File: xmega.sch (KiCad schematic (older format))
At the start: 30 parts, among them J1 USB, J2 PORTA, J4 PORTB, J5 PORTC, J6 PORTE, U1 ATXMEGA128A1U-AU, U5 M24C02-WDW6TP, U6 ADR380

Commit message: Finished?
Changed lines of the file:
@@
 $EndComp
 $Comp
-L GND #PWR3
+L GND #PWR2
 U 1 1 56EBAB34
 P 1300 7400
-F 0 "#PWR3" H 1300 7400 30  0001 C CNN
+F 0 "#PWR2" H 1300 7400 30  0001 C CNN
 F 1 "GND" H 1300 7330 30  0001 C CNN
 F 2 "" H 1300 7400 60  0000 C CNN
@@
 $EndComp
 $Comp
-L GND #PWR21
+L GND #PWR18
 U 1 1 56ECF12E
 P 9950 5000
-F 0 "#PWR21" H 9950 5000 30  0001 C CNN
+F 0 "#PWR18" H 9950 5000 30  0001 C CNN
 F 1 "GND" H 9950 4930 30  0001 C CNN
 F 2 "" H 9950 5000 60  0000 C CNN
@@
 $EndComp
 $Comp
-L +3.3 #PWR20
+L +3.3 #PWR17
 U 1 1 56F51703
 P 9950 4450
-F 0 "#PWR20" H 9950 4500 30  0001 C CNN
+F 0 "#PWR17" H 9950 4500 30  0001 C CNN
 F 1 "+3.3" H 9950 4583 50  0000 C CNN
 F 2 "" H 9950 4450 60  0000 C CNN
@@
 	1150 7200 1300 7200
 Wire Wire Line
-	1300 7200 1300 7300
-Wire Wire Line
-	1300 7300 1300 7400
+	1300 7200 1300 7400
 Wire Wire Line
 	1300 7300 1200 7300
@@
 	9950 5000 9950 4950
 Wire Wire Line
-	7500 3700 7800 3700
-Wire Wire Line
-	7800 3700 8000 3700
+	7500 3700 8000 3700
 Connection ~ 7800 3700
 Wire Wire Line
@@
 	7950 4100 7800 4100
 Wire Wire Line
-	7800 4000 7800 4100
-Wire Wire Line
-	7800 4100 7800 4150
-$Comp
-L GND #PWR30
+	7800 4000 7800 4150
+$Comp
+L GND #PWR15
 U 1 1 56EF0C92
 P 7800 4150
-F 0 "#PWR30" H 7800 4150 30  0001 C CNN
+F 0 "#PWR15" H 7800 4150 30  0001 C CNN
 F 1 "GND" H 7800 4080 30  0001 C CNN
 F 2 "" H 7800 4150 60  0000 C CNN
@@
 	8800 3500 8900 3500
 Wire Wire Line
-	8900 3500 8900 3600
-Wire Wire Line
-	8900 3600 8900 3700
-Wire Wire Line
-	8900 3700 8900 3800
-Wire Wire Line
-	8900 3800 8900 3850
-$Comp
-L GND #PWR40
+	8900 3500 8900 3850
+$Comp
+L GND #PWR16
 U 1 1 56EF1A27
 P 8900 3850
-F 0 "#PWR40" H 8900 3850 30  0001 C CNN
+F 0 "#PWR16" H 8900 3850 30  0001 C CNN
 F 1 "GND" H 8900 3780 30  0001 C CNN
 F 2 "" H 8900 3850 60  0000 C CNN
@@
 P 2400 5300
 AR Path="/56EF5090/56EFEF42" Ref="#PWR?"  Part="1"
-AR Path="/56EFEF42" Ref="#PWR?"  Part="1"
-F 0 "#PWR?" H 2400 5300 30  0001 C CNN
+AR Path="/56EFEF42" Ref="#PWR11"  Part="1"
+F 0 "#PWR11" H 2400 5300 30  0001 C CNN
 F 1 "GND" H 2400 5230 30  0001 C CNN
 F 2 "" H 2400 5300 60  0000 C CNN
@@
 P 2400 4400
 AR Path="/56EF5090/56EFEF48" Ref="#PWR?"  Part="1"
-AR Path="/56EFEF48" Ref="#PWR?"  Part="1"
-F 0 "#PWR?" H 2400 4400 30  0001 C CNN
+AR Path="/56EFEF48" Ref="#PWR10"  Part="1"
+F 0 "#PWR10" H 2400 4400 30  0001 C CNN
 F 1 "GND" H 2400 4330 30  0001 C CNN
 F 2 "" H 2400 4400 60  0000 C CNN
@@
 P 2400 6500
 AR Path="/56EF5090/56EFEF66" Ref="#PWR?"  Part="1"
-AR Path="/56EFEF66" Ref="#PWR?"  Part="1"
-F 0 "#PWR?" H 2400 6500 30  0001 C CNN
+AR Path="/56EFEF66" Ref="#PWR13"  Part="1"
+F 0 "#PWR13" H 2400 6500 30  0001 C CNN
 F 1 "GND" H 2400 6430 30  0001 C CNN
 F 2 "" H 2400 6500 60  0000 C CNN
@@
 P 2400 5600
 AR Path="/56EF5090/56EFEF6C" Ref="#PWR?"  Part="1"
-AR Path="/56EFEF6C" Ref="#PWR?"  Part="1"
-F 0 "#PWR?" H 2400 5600 30  0001 C CNN
+AR Path="/56EFEF6C" Ref="#PWR12"  Part="1"
+F 0 "#PWR12" H 2400 5600 30  0001 C CNN
 F 1 "GND" H 2400 5530 30  0001 C CNN
 F 2 "" H 2400 5600 60  0000 C CNN
@@
 PA7
 $Comp
-L GND #PWR?
+L GND #PWR7
 U 1 1 56EFF0A4
 P 2400 1700
-AR Path="/56EFF0A4" Ref="#PWR?"  Part="1"
+AR Path="/56EFF0A4" Ref="#PWR7"  Part="1"
 AR Path="/56EF5090/56EFF0A4" Ref="#PWR?"  Part="1"
-F 0 "#PWR?" H 2400 1700 30  0001 C CNN
+F 0 "#PWR7" H 2400 1700 30  0001 C CNN
 F 1 "GND" H 2400 1630 30  0001 C CNN
 F 2 "" H 2400 1700 60  0000 C CNN
@@
 $EndComp
 $Comp
-L GND #PWR?
+L GND #PWR6
 U 1 1 56EFF0AA
 P 2400 800
-AR Path="/56EFF0AA" Ref="#PWR?"  Part="1"
+AR Path="/56EFF0AA" Ref="#PWR6"  Part="1"
 AR Path="/56EF5090/56EFF0AA" Ref="#PWR?"  Part="1"
-F 0 "#PWR?" H 2400 800 30  0001 C CNN
+F 0 "#PWR6" H 2400 800 30  0001 C CNN
 F 1 "GND" H 2400 730 30  0001 C CNN
 F 2 "" H 2400 800 60  0000 C CNN
@@
 $EndComp
 $Comp
-L GND #PWR?
+L GND #PWR9
 U 1 1 56EFF0C0
 P 2400 3000
-AR Path="/56EFF0C0" Ref="#PWR?"  Part="1"
+AR Path="/56EFF0C0" Ref="#PWR9"  Part="1"
 AR Path="/56EF5090/56EFF0C0" Ref="#PWR?"  Part="1"
-F 0 "#PWR?" H 2400 3000 30  0001 C CNN
+F 0 "#PWR9" H 2400 3000 30  0001 C CNN
 F 1 "GND" H 2400 2930 30  0001 C CNN
 F 2 "" H 2400 3000 60  0000 C CNN
@@
 $EndComp
 $Comp
-L GND #PWR?
+L GND #PWR8
 U 1 1 56EFF0C6
 P 2400 2100
-AR Path="/56EFF0C6" Ref="#PWR?"  Part="1"
+AR Path="/56EFF0C6" Ref="#PWR8"  Part="1"
 AR Path="/56EF5090/56EFF0C6" Ref="#PWR?"  Part="1"
-F 0 "#PWR?" H 2400 2100 30  0001 C CNN
+F 0 "#PWR8" H 2400 2100 30  0001 C CNN
 F 1 "GND" H 2400 2030 30  0001 C CNN
 F 2 "" H 2400 2100 60  0000 C CNN
@@
 $EndComp
 $Comp
-L GND #PWR?
+L GND #PWR1
 U 1 1 56EFF0E4
 P 900 3750
-AR Path="/56EFF0E4" Ref="#PWR?"  Part="1"
+AR Path="/56EFF0E4" Ref="#PWR1"  Part="1"
 AR Path="/56EF5090/56EFF0E4" Ref="#PWR?"  Part="1"
-F 0 "#PWR?" H 900 3750 30  0001 C CNN
+F 0 "#PWR1" H 900 3750 30  0001 C CNN
 F 1 "GND" H 900 3680 30  0001 C CNN
 F 2 "" H 900 3750 60  0000 C CNN
@@
 $EndComp
 $Comp
-L GND #PWR?
+L GND #PWR3
 U 1 1 56EFF0EA
 P 1400 3750
-AR Path="/56EFF0EA" Ref="#PWR?"  Part="1"
+AR Path="/56EFF0EA" Ref="#PWR3"  Part="1"
 AR Path="/56EF5090/56EFF0EA" Ref="#PWR?"  Part="1"
-F 0 "#PWR?" H 1400 3750 30  0001 C CNN
+F 0 "#PWR3" H 1400 3750 30  0001 C CNN
 F 1 "GND" H 1400 3680 30  0001 C CNN
 F 2 "" H 1400 3750 60  0000 C CNN
@@
 PB0
 $Comp
-L GND #PWR?
+L GND #PWR4
 U 1 1 56EFF10A
 P 1800 4150
-AR Path="/56EFF10A" Ref="#PWR?"  Part="1"
+AR Path="/56EFF10A" Ref="#PWR4"  Part="1"
 AR Path="/56EF5090/56EFF10A" Ref="#PWR?"  Part="1"
-F 0 "#PWR?" H 1800 4150 30  0001 C CNN
+F 0 "#PWR4" H 1800 4150 30  0001 C CNN
 F 1 "GND" H 1800 4080 30  0001 C CNN
 F 2 "" H 1800 4150 60  0000 C CNN
@@
 $EndComp
 $Comp
-L GND #PWR?
+L GND #PWR5
 U 1 1 56EFF118
 P 2250 4150
-AR Path="/56EFF118" Ref="#PWR?"  Part="1"
+AR Path="/56EFF118" Ref="#PWR5"  Part="1"
 AR Path="/56EF5090/56EFF118" Ref="#PWR?"  Part="1"
-F 0 "#PWR?" H 2250 4150 30  0001 C CNN
+F 0 "#PWR5" H 2250 4150 30  0001 C CNN
 F 1 "GND" H 2250 4080 30  0001 C CNN
 F 2 "" H 2250 4150 60  0000 C CNN
@@
 $EndComp
 Wire Wire Line
-	1950 900  2250 900
-Wire Wire Line
-	2250 900  2450 900
+	1950 900  2450 900
 Wire Wire Line
 	2450 1000 1950 1000
@@
 	2400 800  2450 800
 Wire Wire Line
-	1950 2200 2300 2200
-Wire Wire Line
-	2300 2200 2450 2200
+	1950 2200 2450 2200
 Wire Wire Line
 	2450 2300 1950 2300
@@
 	1050 3400 900  3400
 Wire Wire Line
-	900  3300 900  3400
-Wire Wire Line
-	900  3400 900  3500
+	900  3300 900  3500
 Wire Wire Line
 	900  3750 900  3700
@@
 Connection ~ 900  3400
 Wire Wire Line
-	1750 3400 1800 3400
-Wire Wire Line
-	1800 3400 1850 3400
+	1750 3400 1850 3400
 Wire Wire Line
 	1850 3800 1800 3800
 Wire Wire Line
-	1800 3400 1800 3800
-Wire Wire Line
-	1800 3800 1800 3900
+	1800 3400 1800 3900
 Connection ~ 1800 3400
 Wire Wire Line
@@
 	3100 2860 7300 2860
 Wire Wire Line
-	1150 6800 1700 6800
-Wire Wire Line
-	1700 6800 9100 6800
+	1150 6800 9100 6800
 $Comp
 L DRTR5V0U2SR DZ1
@@
 $EndComp
 Wire Wire Line
-	1150 6900 2250 6900
-Wire Wire Line
-	2250 6900 3100 6900
+	1150 6900 3100 6900
 Wire Wire Line
 	3100 7600 3800 7600
@@
 	3800 7700 3000 7700
 Wire Wire Line
-	1150 7000 2150 7000
-Wire Wire Line
-	2150 7000 3000 7000
+	1150 7000 3000 7000
 Wire Wire Line
 	2250 7100 2250 6900
@@
 Connection ~ 1700 6800
 $Comp
-L GND #PWR?
+L GND #PWR14
 U 1 1 56F10850
 P 2700 7500
-F 0 "#PWR?" H 2700 7500 30  0001 C CNN
+F 0 "#PWR14" H 2700 7500 30  0001 C CNN
 F 1 "GND" H 2700 7430 30  0001 C CNN
 F 2 "" H 2700 7500 60  0000 C CNN

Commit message: Reannotate
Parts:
- renumbered C22 to C1, C23 to C2, C29 to C3, DS5 to DS1, J4 to J3, J5 to J4, J6 to J5, R12 to R9, TP3 to TP1, TP5 to TP2, TP6 to TP3, U6 to U2, U5 to U3
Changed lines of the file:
@@
 LD+
 $Comp
-L LED-0603 DS5
+L LED-0603 DS1
 U 1 1 56ED031F
 P 9950 4850
-F 0 "DS5" H 10100 4896 50  0000 L CNN
+F 0 "DS1" H 10100 4896 50  0000 L CNN
 F 1 "PWR" H 10100 4805 50  0000 L CNN
 F 2 "smd-semi:LED-0603" H 9950 4700 50  0001 C CNN
@@
 $EndComp
 $Comp
-L RESPACK-4X0603-CONV R12
+L RESPACK-4X0603-CONV R9
 U 1 1 56F4A476
 P 9950 4550
-F 0 "R12" H 9888 4504 50  0000 R CNN
+F 0 "R9" H 9888 4504 50  0000 R CNN
 F 1 "3k3" H 9888 4595 50  0000 R CNN
 F 2 "IPC7351-Nominal:RESCAXE80P160X320X70-8" H 9950 4550 50  0001 C CNN
@@
 $EndComp
 $Comp
-L C-0402 C29
+L C-0402 C3
 U 1 1 56F56BCD
 P 7800 3900
-F 0 "C29" H 7688 3946 50  0000 R CNN
+F 0 "C3" H 7688 3946 50  0000 R CNN
 F 1 "100n" H 7688 3855 50  0000 R CNN
 F 2 "IPC7351-Nominal:CAPC1005X55" H 7800 3900 50  0001 C CNN
@@
 NoConn ~ 1150 7100
 $Comp
-L 24CXX-SOIC U5
+L 24CXX-SOIC U3
 U 1 1 56EEF028
 P 8400 3650
-F 0 "U5" H 8400 4067 50  0000 C CNN
+F 0 "U3" H 8400 4067 50  0000 C CNN
 F 1 "M24C02-WDW6TP" H 8400 3976 50  0000 C CNN
 F 2 "IPC7351-Nominal:SOP65P640X110-8" H 8400 3650 50  0001 C CNN
@@
 Connection ~ 8900 3600
 $Comp
-L TESTPOINT TP6
+L TESTPOINT TP3
 U 1 1 56EF2C4B
 P 7600 3200
-F 0 "TP6" H 7660 3321 50  0000 L CNN
+F 0 "TP3" H 7660 3321 50  0000 L CNN
 F 1 "SDA" H 7660 3230 50  0000 L CNN
 F 2 "conn-test:TEST-SMD-SMALL" H 7660 3184 50  0001 L CNN
@@
 	7600 3200 7600 3500
 $Comp
-L TESTPOINT TP5
+L TESTPOINT TP2
 U 1 1 56EF3B44
 P 7500 3200
-F 0 "TP5" H 7560 3321 50  0000 L CNN
+F 0 "TP2" H 7560 3321 50  0000 L CNN
 F 1 "SCL" H 7560 3230 50  0000 L CNN
 F 2 "conn-test:TEST-SMD-SMALL" H 7560 3184 50  0001 L CNN
@@
 P 2500 4400
 AR Path="/56EF5090/56EFEF3B" Ref="J?"  Part="1"
-AR Path="/56EFEF3B" Ref="J5"  Part="1"
-F 0 "J5" H 2539 4592 50  0000 C CNN
+AR Path="/56EFEF3B" Ref="J4"  Part="1"
+F 0 "J4" H 2539 4592 50  0000 C CNN
 F 1 "PORTC" H 2539 4501 50  0000 C CNN
 F 2 "conn-100mil:CONN-100MIL-M-1x10" H 2500 4400 50  0001 C CNN
@@
 P 2500 5600
 AR Path="/56EF5090/56EFEF5F" Ref="J?"  Part="1"
-AR Path="/56EFEF5F" Ref="J6"  Part="1"
-F 0 "J6" H 2539 5792 50  0000 C CNN
+AR Path="/56EFEF5F" Ref="J5"  Part="1"
+F 0 "J5" H 2539 5792 50  0000 C CNN
 F 1 "PORTE" H 2539 5701 50  0000 C CNN
 F 2 "conn-100mil:CONN-100MIL-M-1x10" H 2500 5600 50  0001 C CNN
@@
 $EndComp
 $Comp
-L CONN-100MIL-M-1x10 J4
+L CONN-100MIL-M-1x10 J3
 U 1 1 56EFF0B9
 P 2500 2100
-AR Path="/56EFF0B9" Ref="J4"  Part="1"
+AR Path="/56EFF0B9" Ref="J3"  Part="1"
 AR Path="/56EF5090/56EFF0B9" Ref="J?"  Part="1"
-F 0 "J4" H 2539 2292 50  0000 C CNN
+F 0 "J3" H 2539 2292 50  0000 C CNN
 F 1 "PORTB" H 2539 2201 50  0000 C CNN
 F 2 "conn-100mil:CONN-100MIL-M-1x10" H 2500 2100 50  0001 C CNN
@@
 PB7
 $Comp
-L ADR380 U6
+L ADR380 U2
 U 1 1 56EFF0D5
 P 1400 3450
-F 0 "U6" H 1400 3731 50  0000 C CNN
+F 0 "U2" H 1400 3731 50  0000 C CNN
 F 1 "ADR380" H 1400 3640 50  0000 C CNN
 F 2 "smd-semi:SOT-23" H 1400 3450 50  0001 C CNN
@@
 $EndComp
 $Comp
-L C-0402 C22
+L C-0402 C1
 U 1 1 56EFF0DD
 P 900 3600
-AR Path="/56EFF0DD" Ref="C22"  Part="1"
+AR Path="/56EFF0DD" Ref="C1"  Part="1"
 AR Path="/56EF5090/56EFF0DD" Ref="C?"  Part="1"
-F 0 "C22" H 788 3646 50  0000 R CNN
+F 0 "C1" H 788 3646 50  0000 R CNN
 F 1 "100n" H 788 3555 50  0000 R CNN
 F 2 "IPC7351-Nominal:CAPC1005X55" H 900 3600 50  0001 C CNN
@@
 $EndComp
 $Comp
-L C-0402 C23
+L C-0402 C2
 U 1 1 56EFF101
 P 1800 4000
-AR Path="/56EFF101" Ref="C23"  Part="1"
+AR Path="/56EFF101" Ref="C2"  Part="1"
 AR Path="/56EF5090/56EFF101" Ref="C?"  Part="1"
-F 0 "C23" H 1913 4046 50  0000 L CNN
+F 0 "C2" H 1913 4046 50  0000 L CNN
 F 1 "100n" H 1913 3955 50  0000 L CNN
 F 2 "IPC7351-Nominal:CAPC1005X55" H 1800 4000 50  0001 C CNN
@@
 $EndComp
 $Comp
-L TESTPOINT TP3
+L TESTPOINT TP1
 U 1 1 56EFF111
 P 2250 4100
-AR Path="/56EFF111" Ref="TP3"  Part="1"
+AR Path="/56EFF111" Ref="TP1"  Part="1"
 AR Path="/56EF5090/56EFF111" Ref="TP?"  Part="1"
-F 0 "TP3" H 2310 4221 50  0000 L CNN
+F 0 "TP1" H 2310 4221 50  0000 L CNN
 F 1 "GND" H 2310 4130 50  0000 L CNN
 F 2 "manuf:TESTPOINT-KEYSTONE-5018" H 2310 4084 50  0001 L CNN

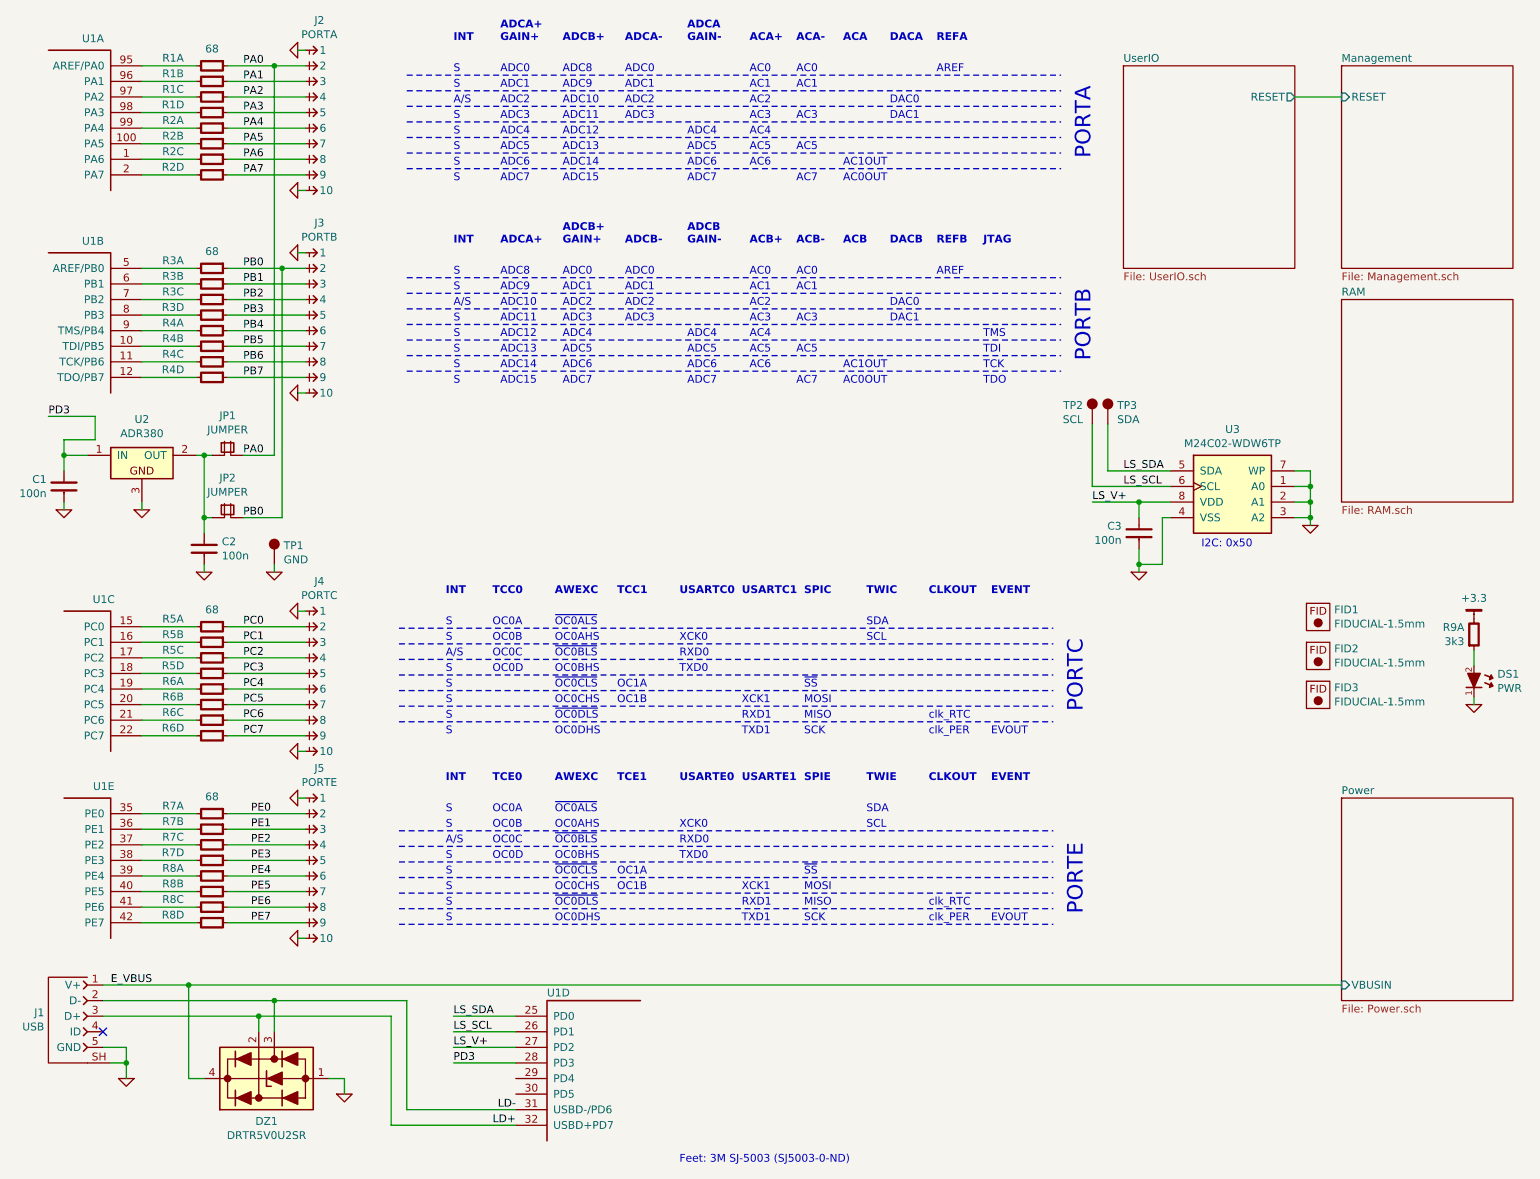
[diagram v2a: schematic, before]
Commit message: Schematic tidy-ups and add VBUS sense
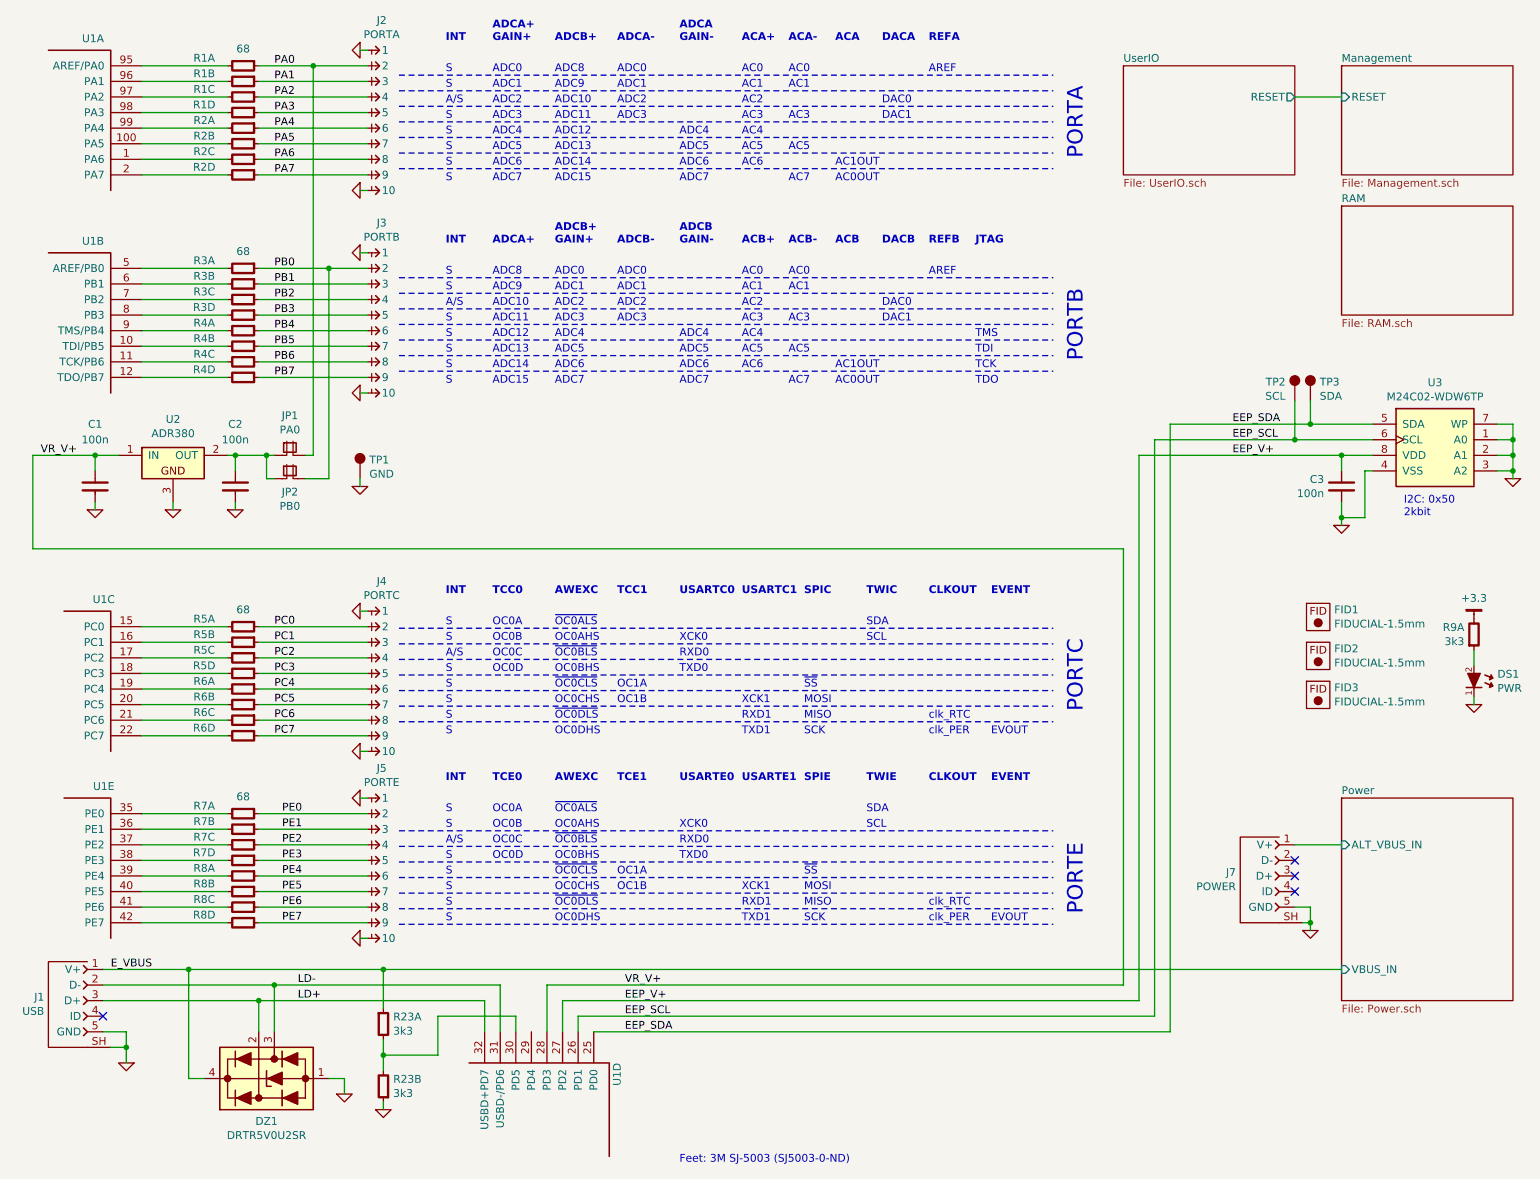
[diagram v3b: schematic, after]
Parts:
- added J7: POWER, conn-fci:CONN-10118194-0001LF-FCI, symbol CONN-10118194-0001LF-UUSB-B
- added R23: 3k3, IPC7351-Nominal:RESCAXE80P160X320X70-8, symbol RESPACK-4X0603-CONV
- JP1: value JUMPER -> PA0
- JP2: value JUMPER -> PB0
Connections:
- net E_VBUS: now also R23.1
- net GND: now also J7.5 (GND), J7.SH (SHIELD), R23.2
- net at U1.30 (PD5): now also R23.7, R23.8
- net LS_SCL renamed EEP_SCL
- net LS_SDA renamed EEP_SDA
- net LS_V+ renamed EEP_V+
- net PD3 renamed VR_V+
- new net Power/ALT_VBUS_IN: J7.1 (V+)
- no-connect marks 1 -> 4
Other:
- note added: "I2C: 0x50\n2kbit"
- note removed: "I2C: 0x50"
- moved on the sheet: C1, C2, C3, J1, J2, J3, J4, J5, JP1, JP2, R1A, R1B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
